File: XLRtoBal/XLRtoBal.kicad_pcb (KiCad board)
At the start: 2 copper layers, 85 x 93 mm, 60 parts, among them J1 XLR4BODYPIN, J10 SMAPCB, J11 SMAPCB, J12 Conn_01x02, J2 Conn_01x04, J3 Conn_01x04, J4 XLR4BODYPIN, J5 Conn_01x04, J6 Conn_01x01, J7 Conn_01x01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

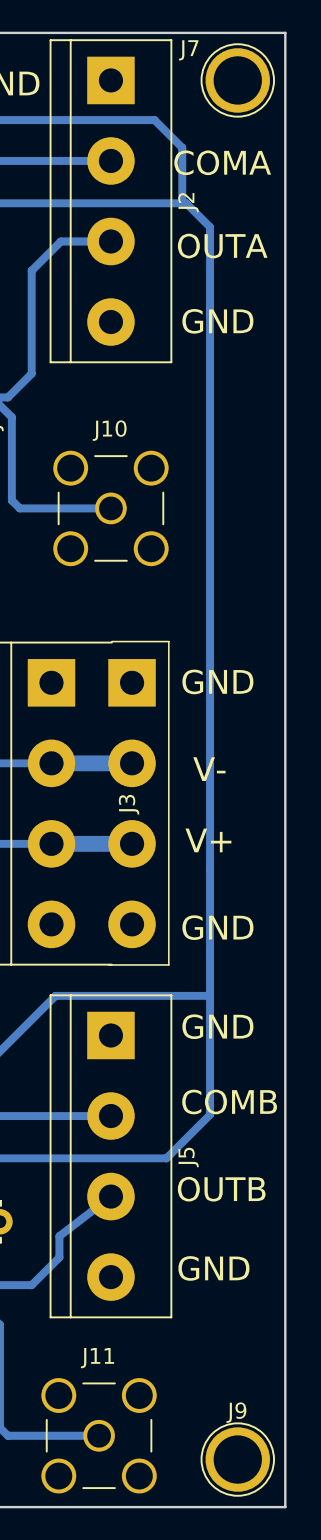
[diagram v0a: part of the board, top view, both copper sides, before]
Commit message: Added OITPC compensation
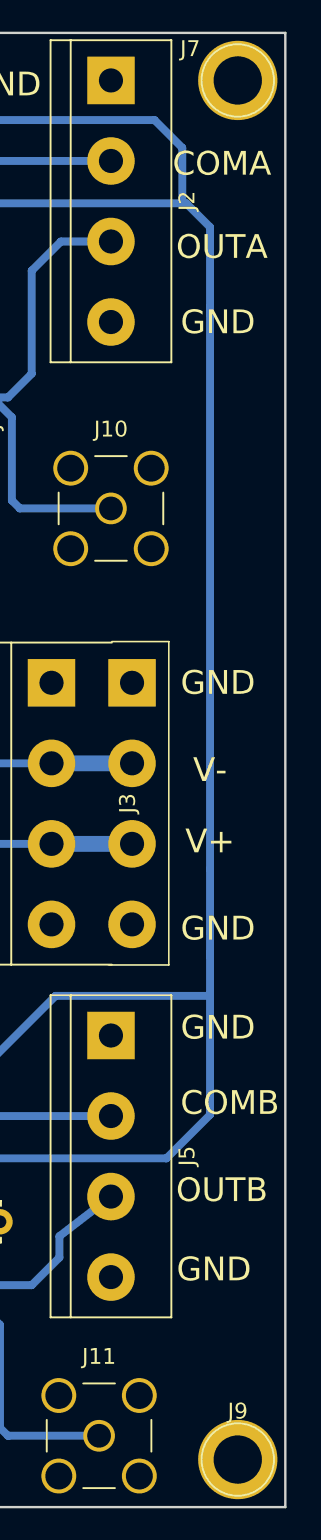
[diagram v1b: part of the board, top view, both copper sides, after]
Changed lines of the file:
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@@
   )
   (setup
-    (last_trace_width 1)
+    (last_trace_width 0.25)
     (user_trace_width 0.35)
     (user_trace_width 0.5)
@@
     (mod_text_size 1 1)
     (mod_text_width 0.15)
-    (pad_size 5.5 5.5)
+    (pad_size 5 5)
     (pad_drill 3.048)
     (pad_to_mask_clearance 0.2)
@@
     (fp_circle (center 0 0) (end 2.6 0) (layer F.CrtYd) (width 0.05))
     (fp_circle (center 0 0) (end 0 -2.286) (layer F.SilkS) (width 0.12))
-    (pad 1 thru_hole circle (at 0 0) (size 4.064 4.064) (drill 3.048) (layers *.Cu *.Mask))
+    (pad "" thru_hole circle (at 0 0) (size 5 5) (drill 3.048) (layers *.Cu *.Mask))
   )
   (module Connectors:1pin (layer F.Cu)
@@
     (fp_circle (center 0 0) (end 2.6 0) (layer F.CrtYd) (width 0.05))
     (fp_circle (center 0 0) (end 0 -2.286) (layer F.SilkS) (width 0.12))
-    (pad 1 thru_hole circle (at 0 0) (size 4.064 4.064) (drill 3.048) (layers *.Cu *.Mask))
+    (pad "" thru_hole circle (at 0 0) (size 5 5) (drill 3.048) (layers *.Cu *.Mask))
   )
   (module Connectors:SMA_THT_Jack_Straight (layer F.Cu)

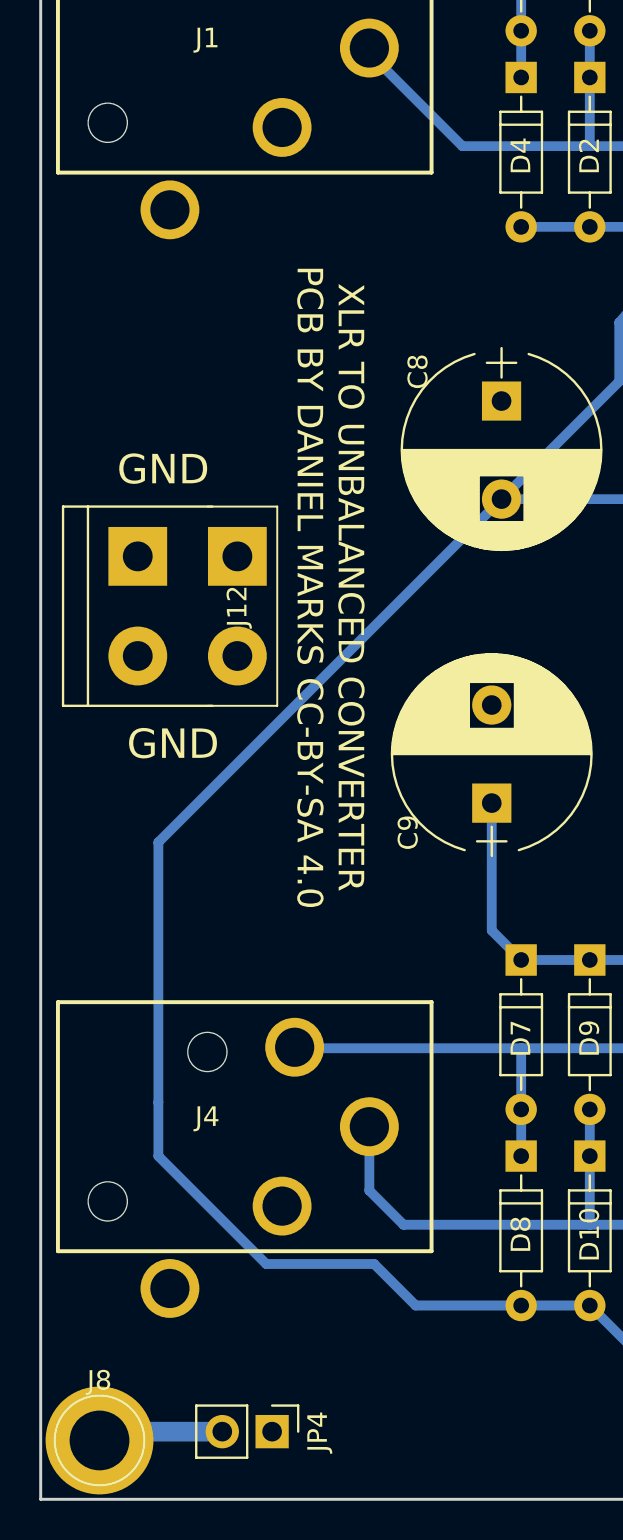
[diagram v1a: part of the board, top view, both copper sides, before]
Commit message: Fixed some silkscreening
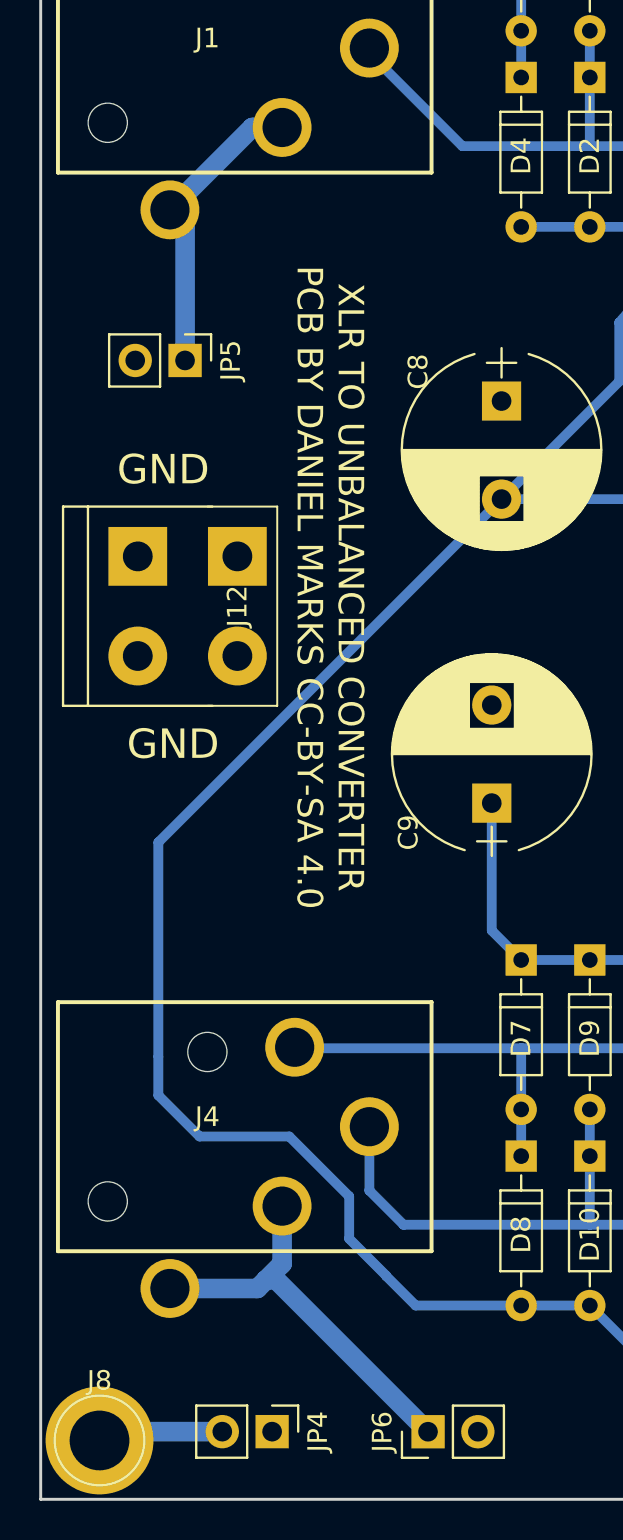
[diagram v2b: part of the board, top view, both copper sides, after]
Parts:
- added JP5: Jumper_NO_Small, Pin_Headers:Pin_Header_Straight_1x02_Pitch2.54mm, F.Cu at (109.4, 93.9)
- added JP6: Jumper_NO_Small, Pin_Headers:Pin_Header_Straight_1x02_Pitch2.54mm, F.Cu at (121.8, 148.6)
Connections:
- J1 pad 1: GND -> Net-(J1-Pad1)
- J1 pad G: GND -> Net-(J1-Pad1)
- J4 pad 1: GND -> Net-(J4-Pad1)
- J4 pad G: GND -> Net-(J4-Pad1)
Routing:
- net Net-(J4-Pad1): track 0.00 -> 20.6 mm
- net Net-(J1-Pad1): track 0.00 -> 15.5 mm
- net VEE: track 174.6 -> 174.1 mm
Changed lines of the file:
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@@
 (kicad_pcb (version 4) (host pcbnew 4.0.7)
   (general
-    (links 123)
+    (links 125)
     (no_connects 0)
     (area 101.924999 58.924999 187.075001 152.075001)
     (thickness 1.6)
     (drawings 25)
-    (tracks 247)
+    (tracks 262)
     (zones 0)
-    (modules 60)
-    (nets 28)
+    (modules 62)
+    (nets 30)
   )
   (page A4)
@@
   )
   (setup
-    (last_trace_width 0.25)
+    (last_trace_width 1)
     (user_trace_width 0.35)
     (user_trace_width 0.5)
@@
   (net 26 "Net-(J6-Pad1)")
   (net 27 "Net-(J8-Pad1)")
+  (net 28 "Net-(J1-Pad1)")
+  (net 29 "Net-(J4-Pad1)")
   (net_class Default "This is the default net class."
     (clearance 0.2)
@@
     (add_net "Net-(D3-Pad2)")
     (add_net "Net-(D7-Pad2)")
+    (add_net "Net-(J1-Pad1)")
     (add_net "Net-(J10-Pad1)")
     (add_net "Net-(J11-Pad1)")
+    (add_net "Net-(J4-Pad1)")
     (add_net "Net-(J6-Pad1)")
     (add_net "Net-(J8-Pad1)")
@@
       (net 9 "Net-(D1-Pad2)"))
     (pad 1 thru_hole circle (at -3.81 -4.05 180) (size 3 3) (drill 2) (layers *.Cu *.Mask)
-      (net 4 GND))
+      (net 28 "Net-(J1-Pad1)"))
     (pad "" np_thru_hole circle (at 5.08 -3.81 180) (size 2 2) (drill 2) (layers *.Cu *.Mask))
     (pad "" np_thru_hole circle (at 0 3.81 180) (size 2 2) (drill 2) (layers *.Cu *.Mask))
@@
       (net 12 "Net-(D3-Pad2)"))
     (pad G thru_hole circle (at 1.91 -8.25 180) (size 3 3) (drill 2) (layers *.Cu *.Mask)
-      (net 4 GND))
+      (net 28 "Net-(J1-Pad1)"))
   )
   (module XLRtoBal:IOXLR3FEH (layer F.Cu)
@@
       (net 21 "Net-(D10-Pad1)"))
     (pad 1 thru_hole circle (at -3.81 -4.05 180) (size 3 3) (drill 2) (layers *.Cu *.Mask)
-      (net 4 GND))
+      (net 29 "Net-(J4-Pad1)"))
     (pad "" np_thru_hole circle (at 5.08 -3.81 180) (size 2 2) (drill 2) (layers *.Cu *.Mask))
     (pad "" np_thru_hole circle (at 0 3.81 180) (size 2 2) (drill 2) (layers *.Cu *.Mask))
@@
       (net 20 "Net-(D7-Pad2)"))
     (pad G thru_hole circle (at 1.91 -8.25 180) (size 3 3) (drill 2) (layers *.Cu *.Mask)
-      (net 4 GND))
+      (net 29 "Net-(J4-Pad1)"))
   )
   (module Capacitors_THT:CP_Radial_D8.0mm_P5.00mm (layer F.Cu)
@@
     )
   )
+  (module Pin_Headers:Pin_Header_Straight_1x02_Pitch2.54mm (layer F.Cu)
+    (at 109.36 93.93 270)
+    (descr "Through hole straight pin header, 1x02, 2.54mm pitch, single row")
+    (tags "Through hole pin header THT 1x02 2.54mm single row")
+    (fp_text reference JP5 (at 0 -2.33 270) (layer F.SilkS)
+      (effects (font (size 1 1) (thickness 0.15)))
+    )
+    (fp_text value Jumper_NO_Small (at 0 4.87 270) (layer F.Fab)
+      (effects (font (size 1 1) (thickness 0.15)))
+    )
+    (fp_line (start -0.635 -1.27) (end 1.27 -1.27) (layer F.Fab) (width 0.1))
+    (fp_line (start 1.27 -1.27) (end 1.27 3.81) (layer F.Fab) (width 0.1))
+    (fp_line (start 1.27 3.81) (end -1.27 3.81) (layer F.Fab) (width 0.1))
+    (fp_line (start -1.27 3.81) (end -1.27 -0.635) (layer F.Fab) (width 0.1))
+    (fp_line (start -1.27 -0.635) (end -0.635 -1.27) (layer F.Fab) (width 0.1))
+    (fp_line (start -1.33 3.87) (end 1.33 3.87) (layer F.SilkS) (width 0.12))
+    (fp_line (start -1.33 1.27) (end -1.33 3.87) (layer F.SilkS) (width 0.12))
+    (fp_line (start 1.33 1.27) (end 1.33 3.87) (layer F.SilkS) (width 0.12))
+    (fp_line (start -1.33 1.27) (end 1.33 1.27) (layer F.SilkS) (width 0.12))
+    (fp_line (start -1.33 0) (end -1.33 -1.33) (layer F.SilkS) (width 0.12))
+    (fp_line (start -1.33 -1.33) (end 0 -1.33) (layer F.SilkS) (width 0.12))
+    (fp_line (start -1.8 -1.8) (end -1.8 4.35) (layer F.CrtYd) (width 0.05))
+    (fp_line (start -1.8 4.35) (end 1.8 4.35) (layer F.CrtYd) (width 0.05))
+    (fp_line (start 1.8 4.35) (end 1.8 -1.8) (layer F.CrtYd) (width 0.05))
+    (fp_line (start 1.8 -1.8) (end -1.8 -1.8) (layer F.CrtYd) (width 0.05))
+    (fp_text user %R (at 0 1.27 360) (layer F.Fab)
+      (effects (font (size 1 1) (thickness 0.15)))
+    )
+    (pad 1 thru_hole rect (at 0 0 270) (size 1.7 1.7) (drill 1) (layers *.Cu *.Mask)
+      (net 28 "Net-(J1-Pad1)"))
+    (pad 2 thru_hole oval (at 0 2.54 270) (size 1.7 1.7) (drill 1) (layers *.Cu *.Mask)
+      (net 4 GND))
+    (model ${KISYS3DMOD}/Pin_Headers.3dshapes/Pin_Header_Straight_1x02_Pitch2.54mm.wrl
+      (at (xyz 0 0 0))
+      (scale (xyz 1 1 1))
+      (rotate (xyz 0 0 0))
+    )
+  )
+  (module Pin_Headers:Pin_Header_Straight_1x02_Pitch2.54mm (layer F.Cu)
+    (at 121.75 148.554 90)
+    (descr "Through hole straight pin header, 1x02, 2.54mm pitch, single row")
+    (tags "Through hole pin header THT 1x02 2.54mm single row")
+    (fp_text reference JP6 (at 0 -2.33 90) (layer F.SilkS)
+      (effects (font (size 1 1) (thickness 0.15)))
+    )
+    (fp_text value Jumper_NO_Small (at 0 4.87 90) (layer F.Fab)
+      (effects (font (size 1 1) (thickness 0.15)))
+    )
+    (fp_line (start -0.635 -1.27) (end 1.27 -1.27) (layer F.Fab) (width 0.1))
+    (fp_line (start 1.27 -1.27) (end 1.27 3.81) (layer F.Fab) (width 0.1))
+    (fp_line (start 1.27 3.81) (end -1.27 3.81) (layer F.Fab) (width 0.1))
+    (fp_line (start -1.27 3.81) (end -1.27 -0.635) (layer F.Fab) (width 0.1))
+    (fp_line (start -1.27 -0.635) (end -0.635 -1.27) (layer F.Fab) (width 0.1))
+    (fp_line (start -1.33 3.87) (end 1.33 3.87) (layer F.SilkS) (width 0.12))
+    (fp_line (start -1.33 1.27) (end -1.33 3.87) (layer F.SilkS) (width 0.12))
+    (fp_line (start 1.33 1.27) (end 1.33 3.87) (layer F.SilkS) (width 0.12))
+    (fp_line (start -1.33 1.27) (end 1.33 1.27) (layer F.SilkS) (width 0.12))
+    (fp_line (start -1.33 0) (end -1.33 -1.33) (layer F.SilkS) (width 0.12))
+    (fp_line (start -1.33 -1.33) (end 0 -1.33) (layer F.SilkS) (width 0.12))
+    (fp_line (start -1.8 -1.8) (end -1.8 4.35) (layer F.CrtYd) (width 0.05))
+    (fp_line (start -1.8 4.35) (end 1.8 4.35) (layer F.CrtYd) (width 0.05))
+    (fp_line (start 1.8 4.35) (end 1.8 -1.8) (layer F.CrtYd) (width 0.05))
+    (fp_line (start 1.8 -1.8) (end -1.8 -1.8) (layer F.CrtYd) (width 0.05))
+    (fp_text user %R (at 0 1.27 180) (layer F.Fab)
+      (effects (font (size 1 1) (thickness 0.15)))
+    )
+    (pad 1 thru_hole rect (at 0 0 90) (size 1.7 1.7) (drill 1) (layers *.Cu *.Mask)
+      (net 29 "Net-(J4-Pad1)"))
+    (pad 2 thru_hole oval (at 0 2.54 90) (size 1.7 1.7) (drill 1) (layers *.Cu *.Mask)
+      (net 4 GND))
+    (model ${KISYS3DMOD}/Pin_Headers.3dshapes/Pin_Header_Straight_1x02_Pitch2.54mm.wrl
+      (at (xyz 0 0 0))
+      (scale (xyz 1 1 1))
+      (rotate (xyz 0 0 0))
+    )
+  )
   (gr_text GND (at 108.75 113.5) (layer F.SilkS)
     (effects (font (size 1.5 1.5) (thickness 0.3)))
@@
   (segment (start 171.54 99.29) (end 172.25 100) (width 0.5) (layer B.Cu) (net 4) (status 30))
   (segment (start 171.46 100.79) (end 172.25 100) (width 0.5) (layer B.Cu) (net 4) (status 30))
+  (segment (start 108 129.43) (end 108 131.4) (width 0.5) (layer B.Cu) (net 5))
+  (segment (start 119.62 140.6) (end 119.62 140.62) (width 0.5) (layer B.Cu) (net 5))
+  (segment (start 117.73 138.71) (end 119.62 140.6) (width 0.5) (layer B.Cu) (net 5))
+  (segment (start 117.73 136.55) (end 117.73 138.71) (width 0.5) (layer B.Cu) (net 5))
+  (segment (start 114.68 133.5) (end 117.73 136.55) (width 0.5) (layer B.Cu) (net 5))
+  (segment (start 110.1 133.5) (end 114.68 133.5) (width 0.5) (layer B.Cu) (net 5))
+  (segment (start 108 131.4) (end 110.1 133.5) (width 0.5) (layer B.Cu) (net 5))
   (segment (start 150.5 142) (end 149.75 142) (width 0.5) (layer B.Cu) (net 5))
   (segment (start 149.75 142) (end 147.25 144.5) (width 0.5) (layer B.Cu) (net 5))
@@
   (segment (start 143.25 101) (end 125.5 101) (width 0.5) (layer B.Cu) (net 5))
   (segment (start 143.75 101.5) (end 143.25 101) (width 0.5) (layer B.Cu) (net 5))
-  (segment (start 108 131.75) (end 108 134.5) (width 0.5) (layer B.Cu) (net 5))
-  (segment (start 108 134.5) (end 113.5 140) (width 0.5) (layer B.Cu) (net 5))
   (segment (start 126.5 142.12) (end 121.12 142.12) (width 0.5) (layer B.Cu) (net 5))
-  (segment (start 121.12 142.12) (end 119 140) (width 0.5) (layer B.Cu) (net 5))
-  (segment (start 119 140) (end 113.5 140) (width 0.5) (layer B.Cu) (net 5))
+  (segment (start 121.12 142.12) (end 119.62 140.62) (width 0.5) (layer B.Cu) (net 5))
   (segment (start 108 118.5) (end 125.5 101) (width 0.5) (layer B.Cu) (net 5))
-  (segment (start 108 131.75) (end 108 118.5) (width 0.5) (layer B.Cu) (net 5))
+  (segment (start 108 129.43) (end 108 118.5) (width 0.5) (layer B.Cu) (net 5))
   (segment (start 153 140.62) (end 151.88 140.62) (width 0.5) (layer B.Cu) (net 5))
   (segment (start 151.88 140.62) (end 150.5 142) (width 0.5) (layer B.Cu) (net 5))
@@
   (segment (start 111.26 148.55) (end 105.45 148.55) (width 1) (layer B.Cu) (net 27))
   (segment (start 105.45 148.55) (end 105 149) (width 1) (layer B.Cu) (net 27))
+  (segment (start 108.59 86.25) (end 108.59 86.3) (width 1) (layer B.Cu) (net 28))
+  (segment (start 108.59 86.3) (end 109.36 87.07) (width 1) (layer B.Cu) (net 28))
+  (segment (start 109.36 87.07) (end 109.36 93.93) (width 1) (layer B.Cu) (net 28))
+  (segment (start 114.31 82.05) (end 112.79 82.05) (width 1) (layer B.Cu) (net 28))
+  (segment (start 112.79 82.05) (end 108.59 86.25) (width 1) (layer B.Cu) (net 28))
+  (segment (start 113.495 140.807) (end 114.003 140.807) (width 1) (layer B.Cu) (net 29))
+  (segment (start 114.003 140.807) (end 121.75 148.554) (width 1) (layer B.Cu) (net 29))
+  (segment (start 114.31 137.05) (end 114.31 139.992) (width 1) (layer B.Cu) (net 29))
+  (segment (start 113.052 141.25) (end 108.59 141.25) (width 1) (layer B.Cu) (net 29))
+  (segment (start 114.31 139.992) (end 113.495 140.807) (width 1) (layer B.Cu) (net 29))
+  (segment (start 113.495 140.807) (end 113.052 141.25) (width 1) (layer B.Cu) (net 29))
   (zone (net 4) (net_name GND) (layer F.Cu) (hatch edge 0.508)
     (connect_pads (clearance 1))

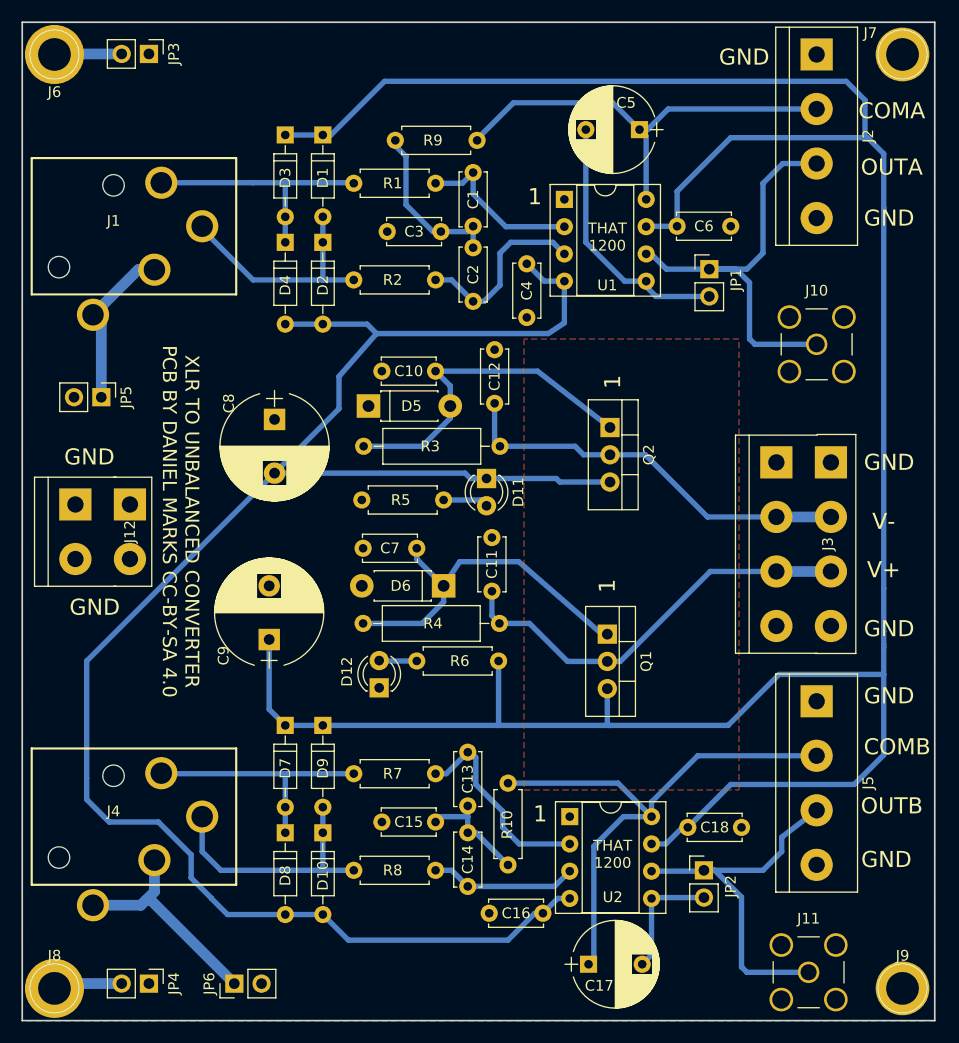
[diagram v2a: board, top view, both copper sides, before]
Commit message: Thickened traces on XLRtoBal board
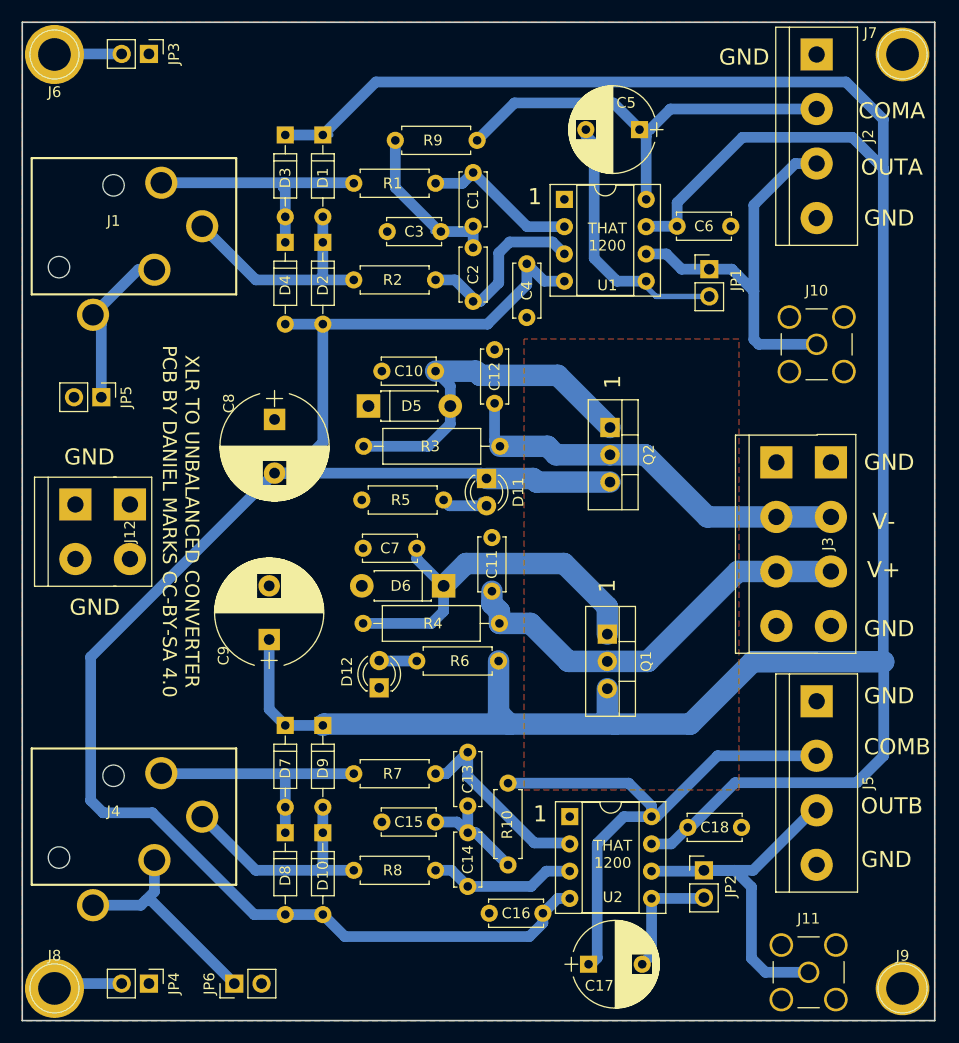
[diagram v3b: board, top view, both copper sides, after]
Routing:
- net VEE: track 174.1 -> 168.4 mm
- net VCC: track 246.1 -> 250.1 mm
- net Net-(C7-Pad2): track 33.6 -> 36.2 mm
- net Net-(J10-Pad1): track 40.3 -> 37.9 mm
- net Net-(C5-Pad1): track 41.7 -> 43.4 mm
- net Net-(D10-Pad1): track 24.0 -> 22.6 mm
- net Net-(C1-Pad2): track 15.7 -> 14.5 mm
- net Net-(C1-Pad1): track 15.9 -> 16.8 mm
- net Net-(C10-Pad1): track 33.9 -> 34.7 mm
- net Net-(D1-Pad2): track 22.2 -> 23.1 mm
- net Net-(C13-Pad2): track 19.2 -> 18.4 mm
- net Net-(D11-Pad2): track 4.22 -> 4.99 mm
- net Net-(C12-Pad1): track 38.5 -> 39.2 mm
- net Net-(C17-Pad1): track 51.7 -> 52.3 mm
